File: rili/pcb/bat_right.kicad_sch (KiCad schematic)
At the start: 21 parts, among them J301 Battery, Q303 AO3407, Q304 FS8205, SW301 SW_SPDT, U303 TP4056-42-ESOP8, U304 MCP1700x-330xxTT, U305 DW01A

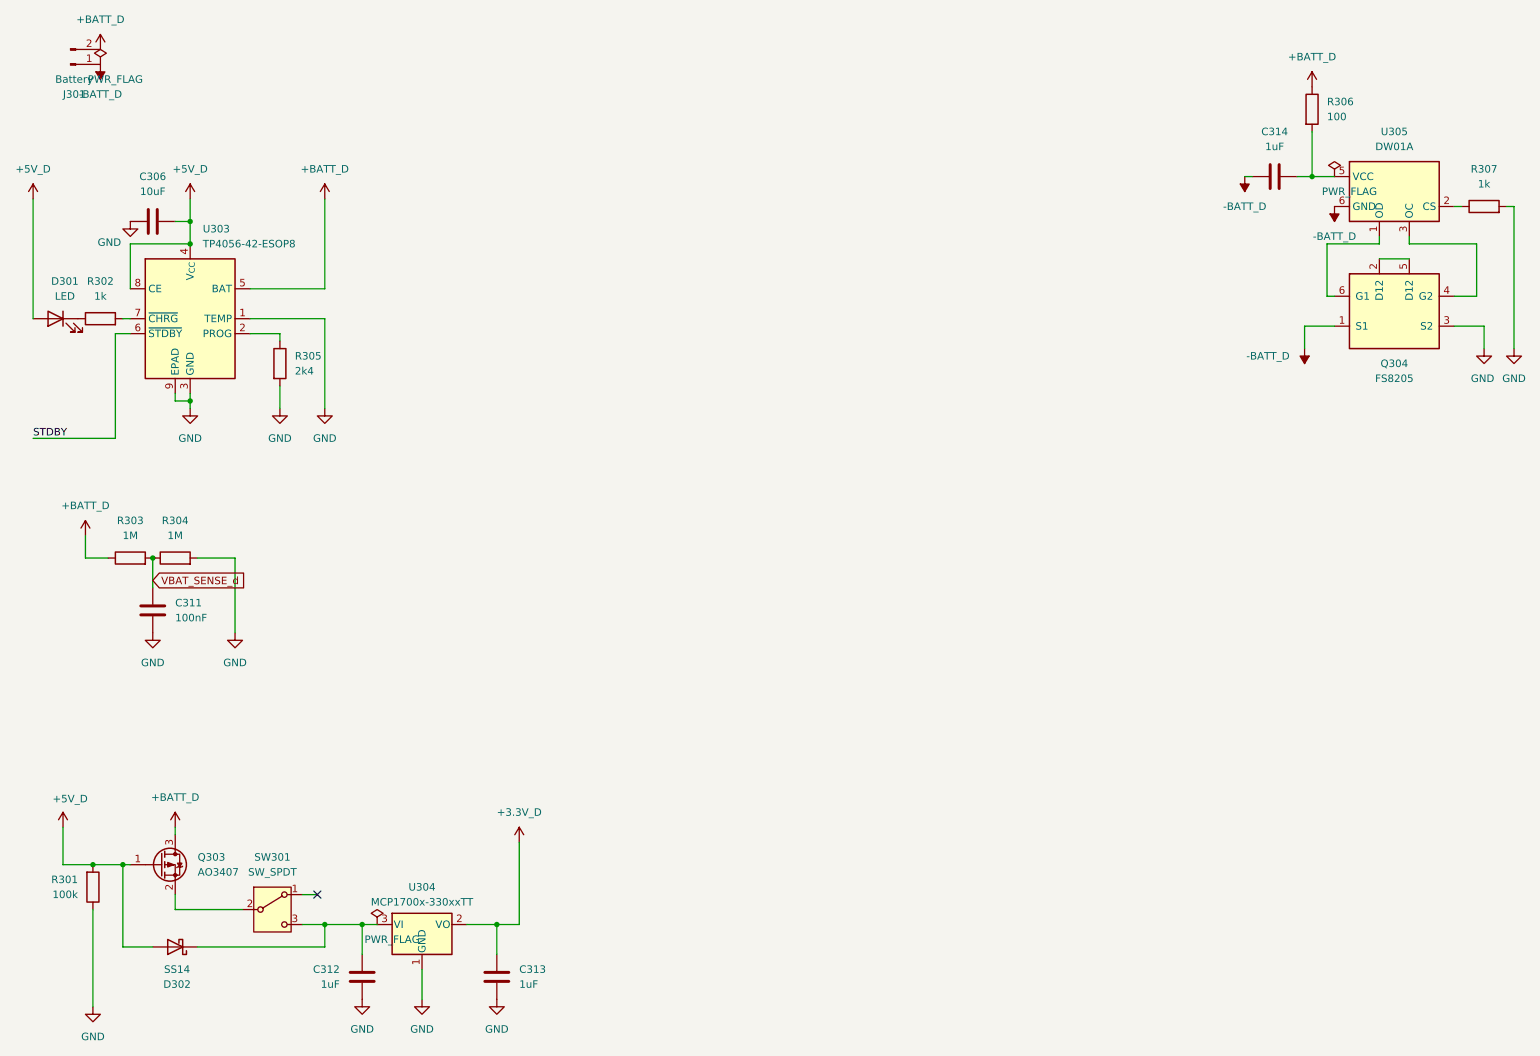
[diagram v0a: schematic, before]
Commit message: layout v2 : carte routée — PCB↔schéma réconciliés, BOM LCSC, TVS matrice, DRC 990→24
- réconciliation PCB↔schéma en une passe : 105 empreintes remariées (matrice ×2,
  module P4), 54 périmées supprimées, ~140 importées par F8 ; footprint TRRS
  MJ-4PP-9_rev3 créé (pads mappés de l'ancien design fonctionnel)
- placement : moitié droite générée au miroir exact du pré-placement gauche
  (axe x=188.46048), trous de montage symétrisés, origine de grille sur l'axe
- protection ESD matrice : 22 SD05C-01F (un par ligne, côté switchs des 100R,
  validés par partition de netlist) ; PWR_FLAG +5V_D réparé
- BOM LCSC dans les propriétés des symboles (32 composants : réfs, liens,
  notes d'achat) + annexe courses complète au plan v2 ; connecteur trackpad
  corrigé (ZIF Hirose FH12-6S-0.5SH, réf MNT Reform)
- règles JLCPCB (planchers DRC + classes Default/Power re-branchées v2),
  passage 4 couches, routage complet des deux moitiés
- gerbers v1 corne-cherry retirés (obsolètes)
- baselines tripwire re-référencées : DRC 990→24 erreurs / 208→17 warnings,
  ERC 0 erreur / 200 warnings (53 fantômes headless documentés)

Co-Authored-By: Claude Fable 5 <noreply@anthropic.com>
Claude-Session: https://claude.ai/code/session_01GfX5RmekmQi78Dm37qsT4Z
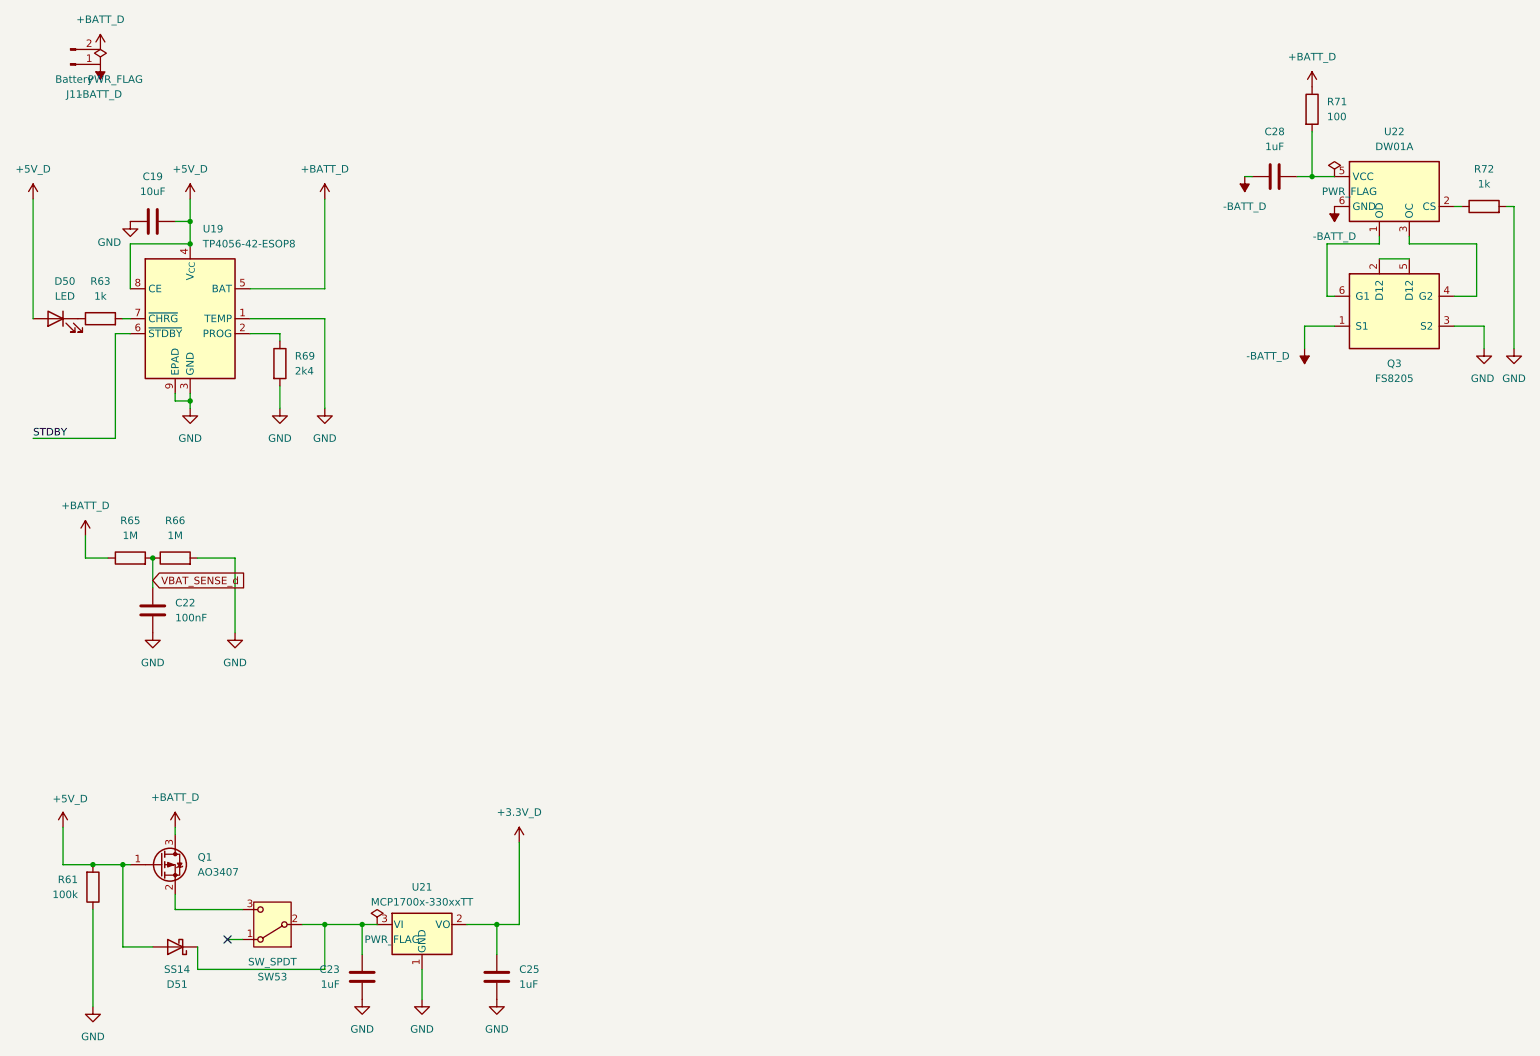
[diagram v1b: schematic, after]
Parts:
- C19: renamed from C306; footprint Capacitor_SMD:C_1210_3225Metric_Pad1.33x2.70mm_HandSolder -> Capacitor_SMD:C_1206_3216Metric_Pad1.33x1.80mm_HandSolder
- D51: renamed from D302; LCSC (none) -> C2480; Lien (none) -> https://lcsc.com/product-detail/C2480.html
- Q1: renamed from Q303; LCSC (none) -> C351408; Lien (none) -> https://lcsc.com/product-detail/C351408.html
- Q3: renamed from Q304; LCSC (none) -> C32254; Lien (none) -> https://lcsc.com/product-detail/C32254.html
- SW53: renamed from SW301; LCSC (none) -> C431540; Lien (none) -> https://lcsc.com/product-detail/C431540.html; Note achat (none) -> MSK-12C02 SHOU HAN
- U19: renamed from U303; LCSC (none) -> C16581; Lien (none) -> https://lcsc.com/product-detail/C16581.html
- U21: renamed from U304; LCSC (none) -> C39051; Lien (none) -> https://lcsc.com/product-detail/C39051.html
- U22: renamed from U305; LCSC (none) -> C351410; Lien (none) -> https://lcsc.com/product-detail/C351410.html
- renumbered C311 to C22, C312 to C23, C313 to C25, C314 to C28, D301 to D50, J301 to J11, R301 to R61, R302 to R63, R303 to R65, R304 to R66, R305 to R69, R306 to R71, R307 to R72
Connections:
- net at C23.2, D51.1 (K), U21.3 (VI): now also SW53.2 (B); no longer SW53.3 (C)
- net at Q1.2 (S): now also SW53.3 (C); no longer SW53.2 (B)
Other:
- moved on the sheet: SW53

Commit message: layout : panneau vertical 2 rails dans le dépôt + baseline chantier
Panneau 185×212 (droite tournée 180°, rails + 8 tabs mouse-bites) appliqué par
Mae, F8 des passifs unifiés. Baseline DRC re-référencée 24/19 → 36/26 (état
panneau, finitions DRC prévues : pistes près des lignes de rupture, vias de
maillage orphelins dans les bandes sans cuivre).

Co-Authored-By: Claude Fable 5 <noreply@anthropic.com>
Claude-Session: https://claude.ai/code/session_01GfX5RmekmQi78Dm37qsT4Z
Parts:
- C22: footprint Capacitor_SMD:C_0805_2012Metric_Pad1.18x1.45mm_HandSolder -> Capacitor_SMD:C_0603_1608Metric
- R61, R71: footprint Resistor_SMD:R_0805_2012Metric_Pad1.20x1.40mm_HandSolder -> Resistor_SMD:R_0603_1608Metric
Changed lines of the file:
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@@
 			)
 		)
-		(property "Footprint" "Capacitor_SMD:C_0805_2012Metric_Pad1.18x1.45mm_HandSolder"
+		(property "Footprint" "Capacitor_SMD:C_0603_1608Metric"
 			(at 39.6748 113.03 0)
 			(hide yes)
@@
 			)
 		)
-		(property "Footprint" "Resistor_SMD:R_0805_2012Metric_Pad1.20x1.40mm_HandSolder"
+		(property "Footprint" "Resistor_SMD:R_0603_1608Metric"
 			(at 235.712 31.75 90)
 			(hide yes)
@@
 			)
 		)
-		(property "Footprint" "Resistor_SMD:R_0805_2012Metric_Pad1.20x1.40mm_HandSolder"
+		(property "Footprint" "Resistor_SMD:R_0603_1608Metric"
 			(at 28.702 163.83 90)
 			(hide yes)

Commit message: review schéma : LDO S3 corrigé (pins SOT-89) + 8 valeurs — HT7833 en place
Revue 4 relecteurs parallèles avant commande, validée ligne à ligne sur la
netlist. BLOQUANT réparé : U20/U21 avaient le brochage SOT-23 du MCP1700 sur
des pastilles SOT-89 → entrée/sortie inversées pour tout LDO réel ; pins 2/3
échangés dans la déf, Value=HT7833 (C50936), F8 + reroutage des 2 zones par
Mae, pads vérifiés (1=GND 2=VIN 3=VOUT). Valeurs : bulk 3V3 C11/C12 et condos
LDO C23-C26 → 10µF (C15850), CHIP_PU P4 R54→10k C14→1µF. Baseline ERC 200→202
(lib_symbol_mismatch des défs LDO éditées). Validé par la revue : chaînes
batterie/charge/load-share, paires USB bout en bout, hub, prog P4 ×2 ports,
microSD IOMUX+pullups, strapping, nRF24, trackpad, 22 TVS matrice.

Co-Authored-By: Claude Fable 5 <noreply@anthropic.com>
Claude-Session: https://claude.ai/code/session_01GfX5RmekmQi78Dm37qsT4Z
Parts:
- C22: footprint Capacitor_SMD:C_0603_1608Metric -> Capacitor_SMD:C_0603_1608Metric_Pad1.08x0.95mm_HandSolder
- C23, C25: value 1uF -> 10uF; footprint Capacitor_SMD:C_0805_2012Metric_Pad1.18x1.45mm_HandSolder -> Capacitor_SMD:C_1206_3216Metric_Pad1.33x1.80mm_HandSolder
- R61, R71: footprint Resistor_SMD:R_0603_1608Metric -> Resistor_SMD:R_0603_1608Metric_Pad0.98x0.95mm_HandSolder
- U21: value MCP1700x-330xxTT -> HT7833; LCSC C39051 -> C50936; Lien https://lcsc.com/product-detail/C39051.html -> https://lcsc.com/product-detail/C50936.html
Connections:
- net +3.3V_D: now also U21.3 (VO); no longer U21.2 (VO)
- net at C23.2, D51.1 (K), SW53.2 (B): now also U21.2 (VI); no longer U21.3 (VI)
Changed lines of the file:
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@@
 			)
 		)
-		(property "Value" "1uF"
+		(property "Value" "10uF"
 			(at 102.87 180.3399 0)
 			(show_name no)
@@
 			)
 		)
-		(property "Footprint" "Capacitor_SMD:C_0805_2012Metric_Pad1.18x1.45mm_HandSolder"
+		(property "Footprint" "Capacitor_SMD:C_1206_3216Metric_Pad1.33x1.80mm_HandSolder"
 			(at 98.0948 175.26 0)
 			(hide yes)
@@
 			)
 		)
-		(property "Value" "1uF"
+		(property "Value" "10uF"
 			(at 72.39 180.3399 0)
 			(show_name no)
@@
 			)
 		)
-		(property "Footprint" "Capacitor_SMD:C_0805_2012Metric_Pad1.18x1.45mm_HandSolder"
+		(property "Footprint" "Capacitor_SMD:C_1206_3216Metric_Pad1.33x1.80mm_HandSolder"
 			(at 77.1652 175.26 0)
 			(hide yes)
@@
 			)
 		)
-		(property "Footprint" "Capacitor_SMD:C_0603_1608Metric"
+		(property "Footprint" "Capacitor_SMD:C_0603_1608Metric_Pad1.08x0.95mm_HandSolder"
 			(at 39.6748 113.03 0)
 			(hide yes)
@@
 			)
 		)
-		(property "Value" "MCP1700x-330xxTT"
+		(property "Value" "HT7833"
 			(at 86.36 166.37 0)
 			(show_name no)
@@
 			)
 		)
-		(property "LCSC" "C39051"
+		(property "LCSC" "C50936"
 			(at 86.36 170.18 0)
 			(hide yes)
@@
 			)
 		)
-		(property "Lien" "https://lcsc.com/product-detail/C39051.html"
+		(property "Lien" "https://lcsc.com/product-detail/C50936.html"
 			(at 86.36 170.18 0)
 			(hide yes)
@@
 			)
 		)
-		(property "Footprint" "Resistor_SMD:R_0603_1608Metric"
+		(property "Footprint" "Resistor_SMD:R_0603_1608Metric_Pad0.98x0.95mm_HandSolder"
 			(at 235.712 31.75 90)
 			(hide yes)
@@
 			)
 		)
-		(property "Footprint" "Resistor_SMD:R_0603_1608Metric"
+		(property "Footprint" "Resistor_SMD:R_0603_1608Metric_Pad0.98x0.95mm_HandSolder"
 			(at 28.702 163.83 90)
 			(hide yes)
